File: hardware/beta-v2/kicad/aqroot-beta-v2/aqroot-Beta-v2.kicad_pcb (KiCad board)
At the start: 6 copper layers, 72 x 148 mm, 324 parts, among them J1 FH69-50S-0.5SH, J2 Molex_5025700893, J3 USB_C_Receptacle_USB2.0_16P, J4 JST-PH-2 BATTERY, J5 COMMUNITY_PORT_1x24, J6 JST-PH-2 SPEAKER, J7 BM02B-ACHSS-GAN-ETF, J8 QWIIC_STEMMA_QT, Q1 AO3400A, Q10 2N7002, Q2 NTMD4820N, Q3 NTMD4820N, Q4 BSS138, Q5 AO3401A, Q6 BSS138, Q7 BSS138, Q8 BSS138, Q9 BSS138, SW1 BOOT, SW2 UP, SW3 DOWN, SW4 LEFT, SW5 RIGHT, SW6 A_SELECT, SW7 B_BACK, SW9 SW_SPDT, U1 ESP32-S3-WROOM-1, U10 USBLC6-2SC6, U11 BQ25185, U12 TPS63020, U13 TPS61023, U14 MAX17048, U16 TCA4307DGKR, U17 TPS61169DCKR, U18 LTC4368-1, U19 TLV7032, U2 PCAL9535APW, U20 TPS22950C, U21 TPS61023, U22 TPS22950C, U23 PCAL9535APW, U3 PCAL9535APW, U4 BMI270, U5 MAX98357A, U6 TSOP38238, U7 E07-400M10S, U8 E22-900M22S, U9 ST25R3916-AQET, Y1 27.12MHz 10pF 3225-4P

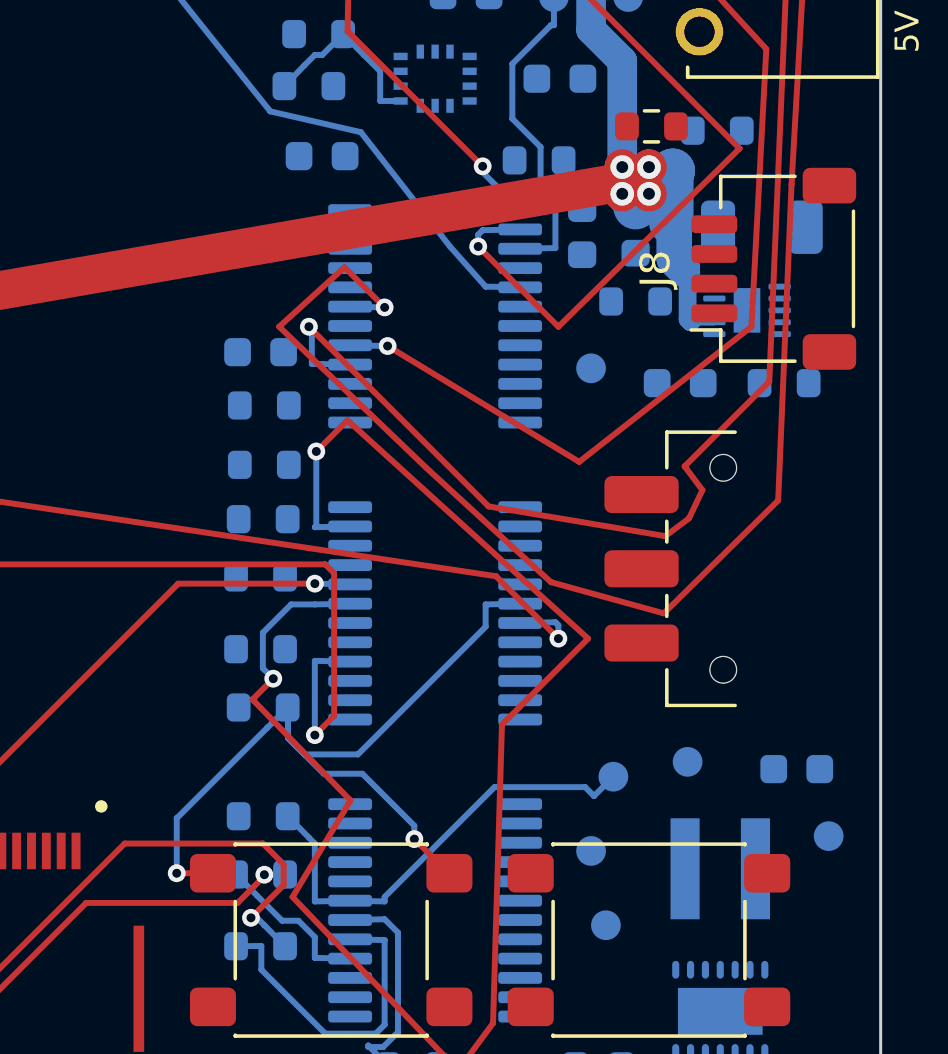
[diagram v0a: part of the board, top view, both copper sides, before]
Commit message: FBV2-P2-028: D-326 TWENTIETH REST-OF-BOARD INCREMENT — BTN_UP_N PROMOTED (second SWx user button, cleaner than BTN_B_N, ZERO router-logic change)
The navigation D-pad UP button BTN_UP_N routed and PROMOTED on the accepted D-325
duplicate-ref MST framework — a GROUPS registry entry + comment only, no routing-
logic change (physical_net_pads/net_open_edges/qrouter.py byte-identical to D-325,
so router_regression G1-G37 stay byte-identical). CLEANER than BTN_B_N: ONE through
via, not two. AUTH 35d32343...(800/70/662/119) -> adbea36b8bbcfa393f2810e989c93dbcfab4052b5538f9a7169bc71ff98b3e3f (821/71/659/122).

MANDATE-SHA NOTE: the mandate quoted the pre-work sha as 35d32343af5146b973f5231e76d252e90ddf796d274e63200da5ea41e5767ea7; the live board, live_fingerprint.py, the D-325 commit and CURRENT_STATE all agree the true D-325 sha is 35d32343af5146b952e5390898764fd326742dc88b5e146cf0c5f292dc14a220 (they share only the 16-char abbreviation prefix). The live board hashed byte-for-byte to the repo's own single-source-of-truth value, so work proceeded on that verified basis; the mandate tail was a transcription artifact, not a board discrepancy.

CANDIDATE SCREEN (read-only, live D-325 board). Every remaining SWx nav button shares BTN_B_N's topology: its switch (SW2-SW6) is the SAME 4-pin PTS645 tact switch whose two mechanically-linked terminals BOTH carry pad number "1" (7.96 mm apart), plus a B.Cu pull-up (R4-R8) and a B.Cu PCAL9535A expander GPIO (U2.13-U2.17). Two independent screens (w/screen_020.py bbox congestion + a faithful physical_net_pads/mst_edges route-plan vet) measured all five; BTN_UP_N is decisively cleanest — cross-haul 12.33 mm / cong 201 (vs BTN_A 42.35/429, BTN_DOWN 44.00/352, BTN_LEFT 50.15/568, BTN_RIGHT 56.89/508) — because SW2 sits in the SAME open south button field where BTN_B_N (SW7) already passed. Every nav button is a 1-via increment (its two F.Cu switch lands join by a same-layer F.Cu land-run — the D-325 lever edge — so only the haul to the R/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
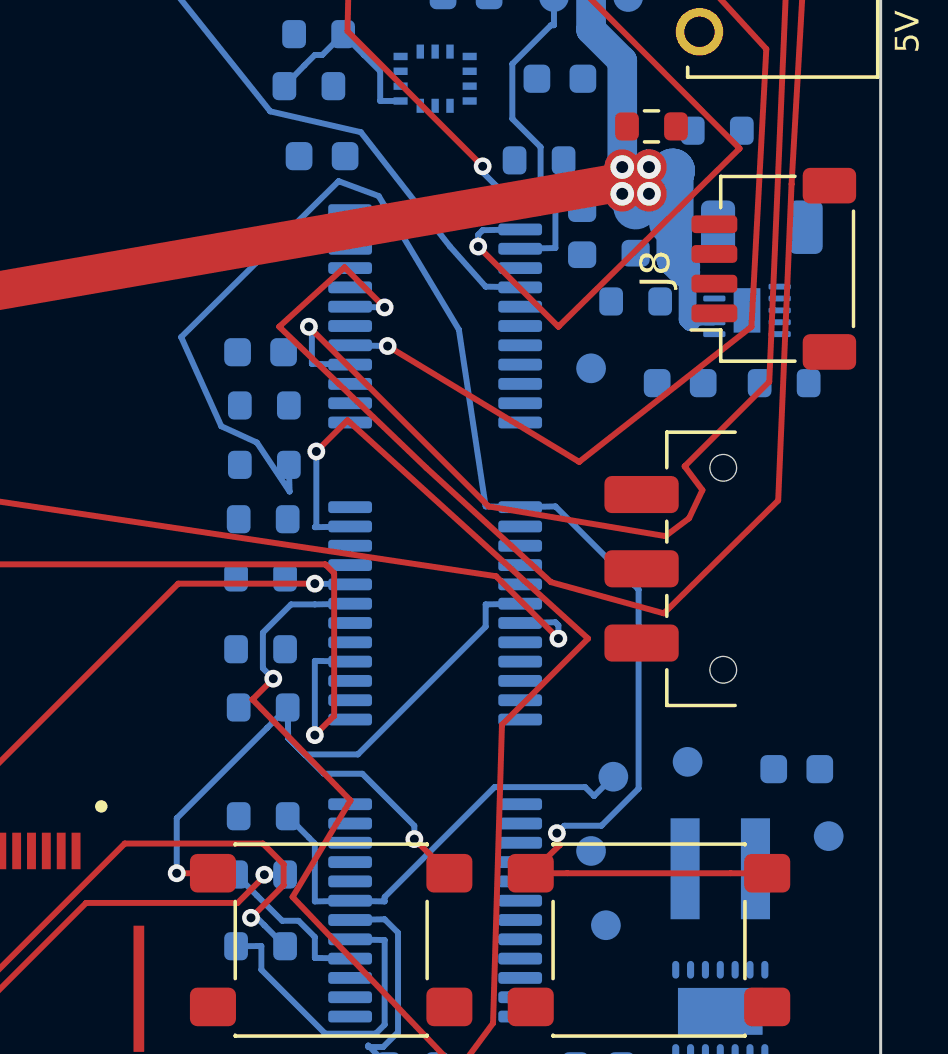
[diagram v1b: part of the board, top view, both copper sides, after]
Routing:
- net /08_BUTTONS_EXPANDERS/BTN_UP_N: track 0.00 -> 53.8 mm, vias 0 -> 1
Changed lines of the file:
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@@
+	)
+	(segment
+		(start 60.22 96.75)
+		(end 61.2 95.8)
+		(width 0.2)
+		(layer "F.Cu")
+		(net "/08_BUTTONS_EXPANDERS/BTN_UP_N")
+	)
+	(segment
+		(start 61.2 95.8)
+		(end 61.1 95.7)
+		(width 0.2)
+		(layer "F.Cu")
+		(net "/08_BUTTONS_EXPANDERS/BTN_UP_N")
+	)
+	(segment
+		(start 68.18 96.75)
+		(end 66.95 96.75)
+		(width 0.2)
+		(layer "F.Cu")
+		(net "/08_BUTTONS_EXPANDERS/BTN_UP_N")
+	)
+	(segment
+		(start 60.22 96.75)
+		(end 61.45 96.75)
+		(width 0.2)
+		(layer "F.Cu")
+		(net "/08_BUTTONS_EXPANDERS/BTN_UP_N")
+	)
+	(segment
+		(start 61.1 95.7)
+		(end 61.1 95.4)
+		(width 0.2)
+		(layer "F.Cu")
+		(net "/08_BUTTONS_EXPANDERS/BTN_UP_N")
+	)
+	(segment
+		(start 61.45 96.75)
+		(end 66.95 96.75)
+		(width 0.2)
+		(layer "F.Cu")
+		(net "/08_BUTTONS_EXPANDERS/BTN_UP_N")
+	)
+	(via
+		(at 61.1 95.4)
+		(size 0.6)
+		(drill 0.3)
+		(layers "F.Cu" "B.Cu")
+		(net "/08_BUTTONS_EXPANDERS/BTN_UP_N")
+	)
+	(segment
+		(start 51 82.25)
+		(end 49.8 81.7)
+		(width 0.2)
+		(layer "B.Cu")
+		(net "/08_BUTTONS_EXPANDERS/BTN_UP_N")
+	)
+	(segment
+		(start 57.8 78.45)
+		(end 58.7 84.4)
+		(width 0.2)
+		(layer "B.Cu")
+		(net "/08_BUTTONS_EXPANDERS/BTN_UP_N")
+	)
+	(segment
+		(start 62.6 95.15)
+		(end 61.35 95.15)
+		(width 0.2)
+		(layer "B.Cu")
+		(net "/08_BUTTONS_EXPANDERS/BTN_UP_N")
+	)
+	(segment
+		(start 52.075 83)
+		(end 52.1 83.9)
+		(width 0.2)
+		(layer "B.Cu")
+		(net "/08_BUTTONS_EXPANDERS/BTN_UP_N")
+	)
+	(segment
+		(start 59.8625 84.425)
+		(end 58.7 84.4)
+		(width 0.2)
+		(layer "B.Cu")
+		(net "/08_BUTTONS_EXPANDERS/BTN_UP_N")
+	)
+	(segment
+		(start 53.75 73.45)
+		(end 55.1 73.95)
+		(width 0.2)
+		(layer "B.Cu")
+		(net "/08_BUTTONS_EXPANDERS/BTN_UP_N")
+	)
+	(segment
+		(start 55.1 73.95)
+		(end 57.8 78.45)
+		(width 0.2)
+		(layer "B.Cu")
+		(net "/08_BUTTONS_EXPANDERS/BTN_UP_N")
+	)
+	(segment
+		(start 61.35 95.15)
+		(end 61.1 95.4)
+		(width 0.2)
+		(layer "B.Cu")
+		(net "/08_BUTTONS_EXPANDERS/BTN_UP_N")
+	)
+	(segment
+		(start 59.8625 84.425)
+		(end 61.05 84.4)
+		(width 0.2)
+		(layer "B.Cu")
+		(net "/08_BUTTONS_EXPANDERS/BTN_UP_N")
+	)
+	(segment
+		(start 48.45 78.7)
+		(end 53.75 73.45)
+		(width 0.2)
+		(layer "B.Cu")
+		(net "/08_BUTTONS_EXPANDERS/BTN_UP_N")
+	)
+	(segment
+		(start 49.8 81.7)
+		(end 48.45 78.7)
+		(width 0.2)
+		(layer "B.Cu")
+		(net "/08_BUTTONS_EXPANDERS/BTN_UP_N")
+	)
+	(segment
+		(start 61.05 84.4)
+		(end 63.85 87.2)
+		(width 0.2)
+		(layer "B.Cu")
+		(net "/08_BUTTONS_EXPANDERS/BTN_UP_N")
+	)
+	(segment
+		(start 52.1 83.9)
+		(end 51 82.25)
+		(width 0.2)
+		(layer "B.Cu")
+		(net "/08_BUTTONS_EXPANDERS/BTN_UP_N")
+	)
+	(segment
+		(start 63.85 93.9)
+		(end 62.6 95.15)
+		(width 0.2)
+		(layer "B.Cu")
+		(net "/08_BUTTONS_EXPANDERS/BTN_UP_N")
+	)
+	(segment
+		(start 63.85 87.2)
+		(end 63.85 93.9)
+		(width 0.2)
+		(layer "B.Cu")
+		(net "/08_BUTTONS_EXPANDERS/BTN_UP_N")
 	)
 	(segment
